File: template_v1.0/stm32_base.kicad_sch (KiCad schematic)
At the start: 41 parts, among them J1 Network Connector, J2 STDC14, SW1 SW_Push, U1 LD39050PU33R, U2 STM32G474RBT6, U3 SN65HVD230, Y1 8MHz

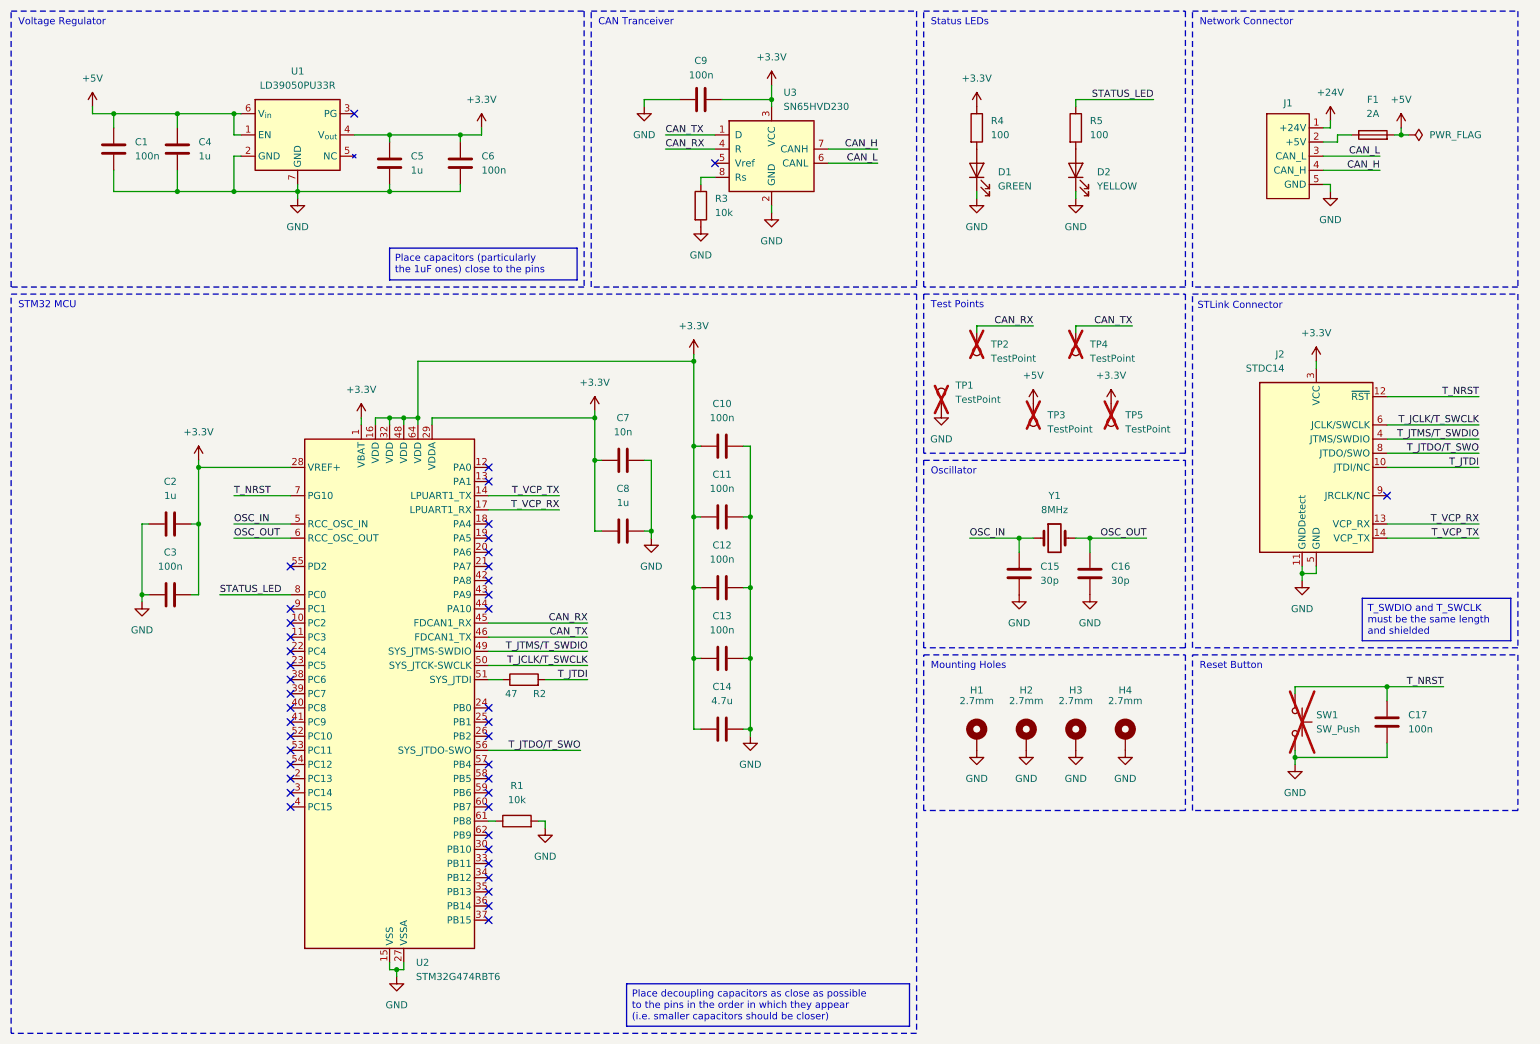
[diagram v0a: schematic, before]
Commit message: Exo-template-pcb : Add new protective diodes/
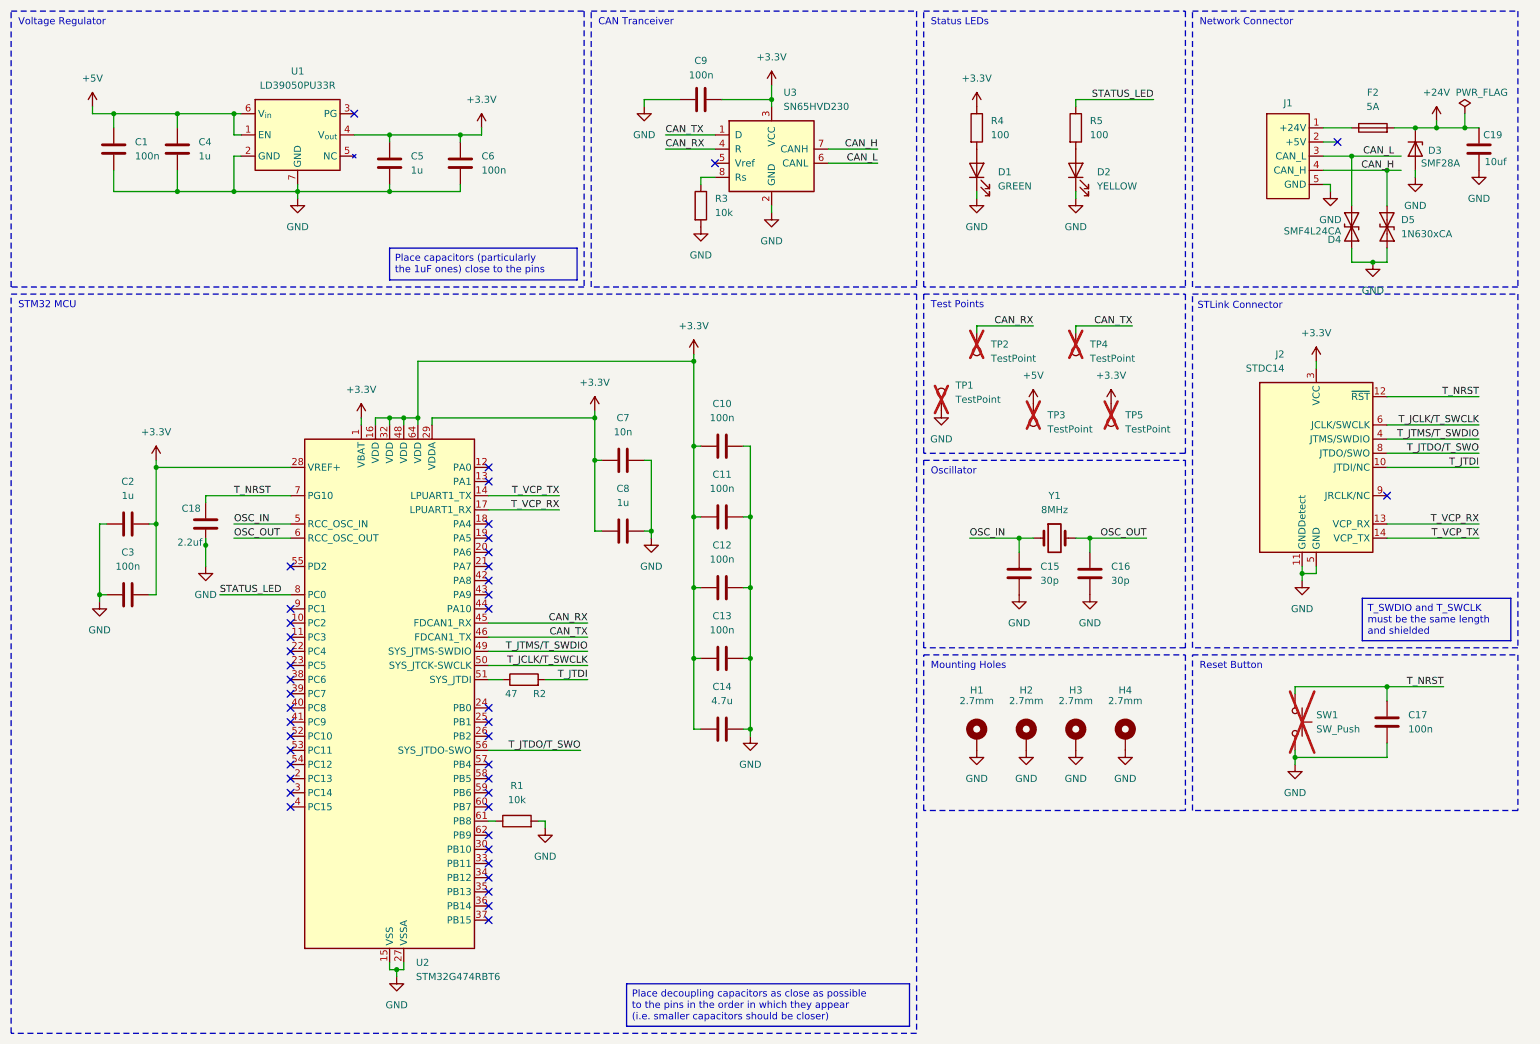
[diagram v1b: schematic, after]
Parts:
- removed F1: 2A, Exocet:Fuse_Holder_Littelfuse_01530008, symbol Device:Fuse
- added C18: 2.2uf, Capacitor_SMD:C_01005_0402Metric, symbol Device:C
- added C19: 10uf, Capacitor_SMD:C_0805_2012Metric, symbol Device:C
- added D3: SMF28A, Diode_SMD:D_SOD-123F, symbol Device:D_Zener
- added D4: SMF4L24CA, Diode_SMD:D_SOD-123F, symbol Diode:1N630xCA
- added D5: 1N630xCA, Diode_SMD:D_SOD-123F, symbol Diode:1N630xCA
- added F2: 5A, Exocet:Fuse_Holder_Littelfuse_01530008, symbol Device:Fuse
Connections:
- net +24V: now also C19.1, D3.1 (K), F2.2; no longer J1.1 (+24V)
- net CAN_H: now also D5.2 (A2)
- net CAN_L: now also D4.2 (A2)
- net GND: now also C18.2, C19.2, D3.2 (A), D4.1 (A1), D5.1 (A1)
- net T_NRST: now also C18.1
- new net: F2.1, J1.1 (+24V)
- no-connect marks 42 -> 43
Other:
- moved on the sheet: C2, C3

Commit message: Exo-template-pcb : Add ferrite bead and footprints
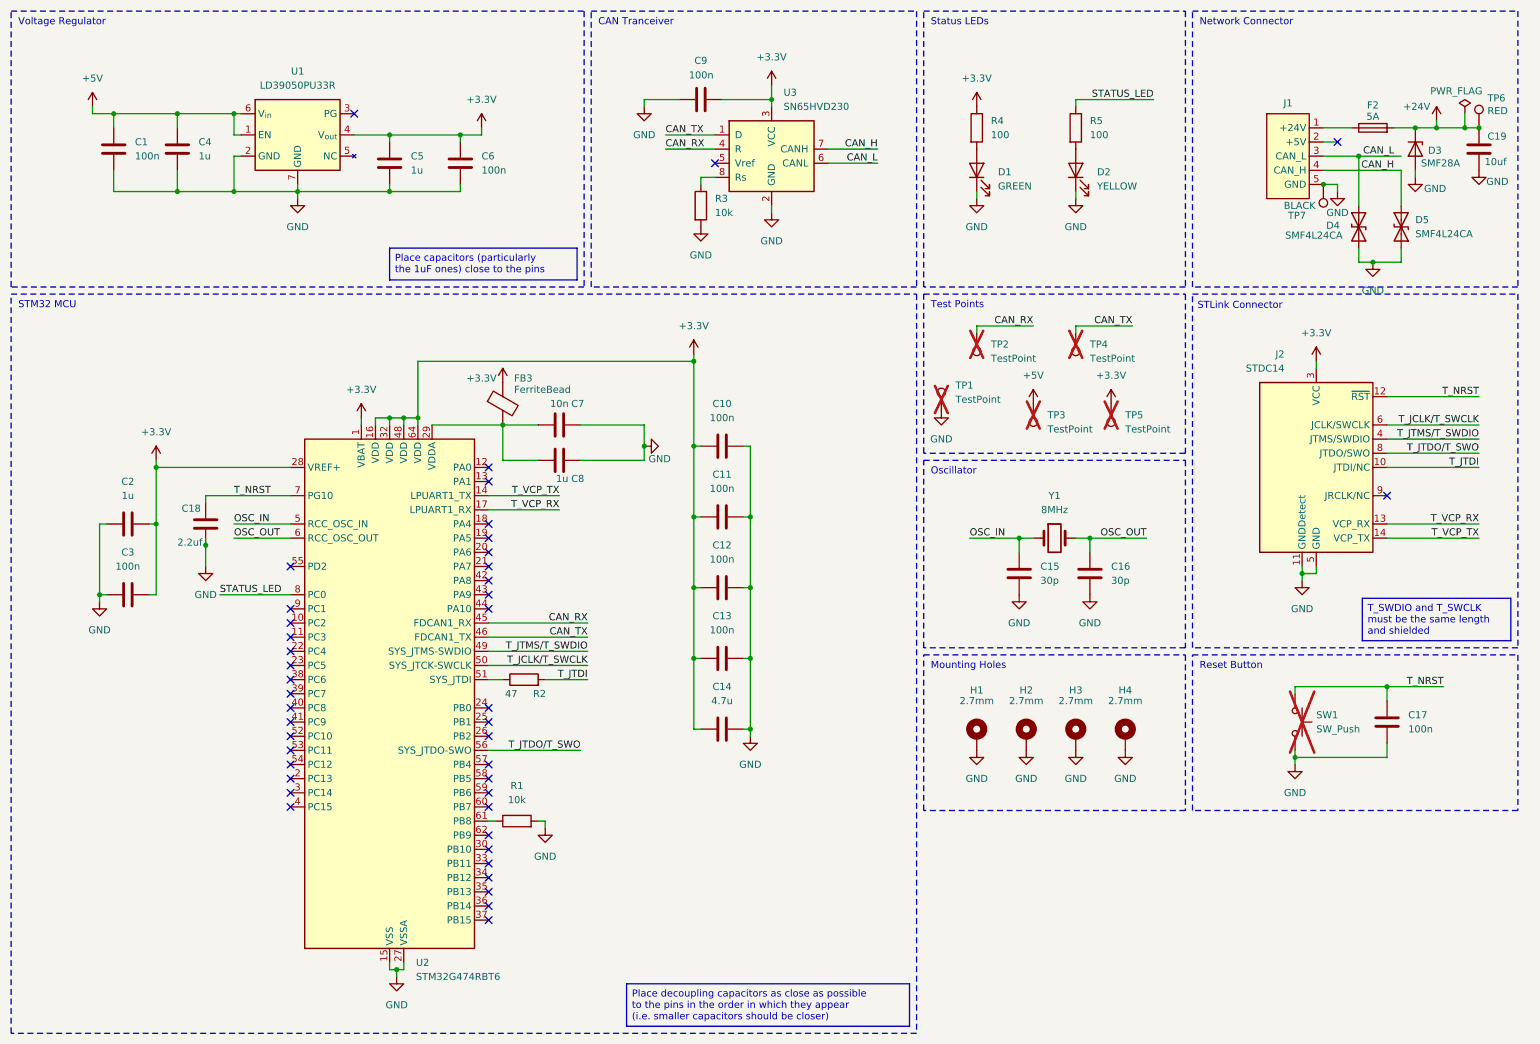
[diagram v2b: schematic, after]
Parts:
- added FB3: FerriteBead, Resistor_SMD:R_0805_2012Metric, symbol Device:FerriteBead
- added TP6: RED, Package_TO_SOT_SMD:SOT-23-5, symbol Connector:TestPoint
- added TP7: BLACK, symbol Connector:TestPoint
- C18: JLCPCB (none) -> C12530
- D3: JLCPCB (none) -> C41376091
- D4: JLCPCB (none) -> C53278608
- D5: value 1N630xCA -> SMF4L24CA; JLCPCB (none) -> C53278608
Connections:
- net +24V: now also TP6.1
- net +3.3V: now also FB3.1; no longer C7.1, C8.1, U2.29 (VDDA)
- net GND: now also TP7.1
- new net: C7.1, C8.1, FB3.2, U2.29 (VDDA)
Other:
- moved on the sheet: C7, C8, D4, D5

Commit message: Exo-template-pcb : Add regulator 3.3V
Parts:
- removed C1, C6: 100n, Capacitor_SMD:C_0402_1005Metric, symbol Device:C
- removed U1: LD39050PU33R, Package_DFN_QFN:DFN-6-1EP_3x3mm_P0.95mm_EP1.7x2.6mm, symbol Exocet:LD39050PU33R
- added U4: LM3940, Package_TO_SOT_THT:TO-220-3_Vertical, symbol Exocet:LM3940
- C4: value 1u -> 0.47u
- C5: value 1u -> 47u
- F2: value 5A -> 7.5A
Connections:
- net +3.3V: now also U4.3 (VO)
- net +5V: now also U4.1 (VI)
- net GND: now also U4.2 (GND)
- no-connect marks 43 -> 42
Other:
- moved on the sheet: C4, C5
